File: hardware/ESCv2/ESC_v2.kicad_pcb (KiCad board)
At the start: 4 copper layers, 99.1 x 49.5 mm, 57 parts, among them J1 Conn_02x13_Odd_Even, J2 Conn_01x02, Q1 AON7544, Q2 AON7544, Q3 AON7544, Q4 AON7544, Q5 AON7544, Q6 AON7544, U1 MT6701CT, U2 DRV8305NPHPR

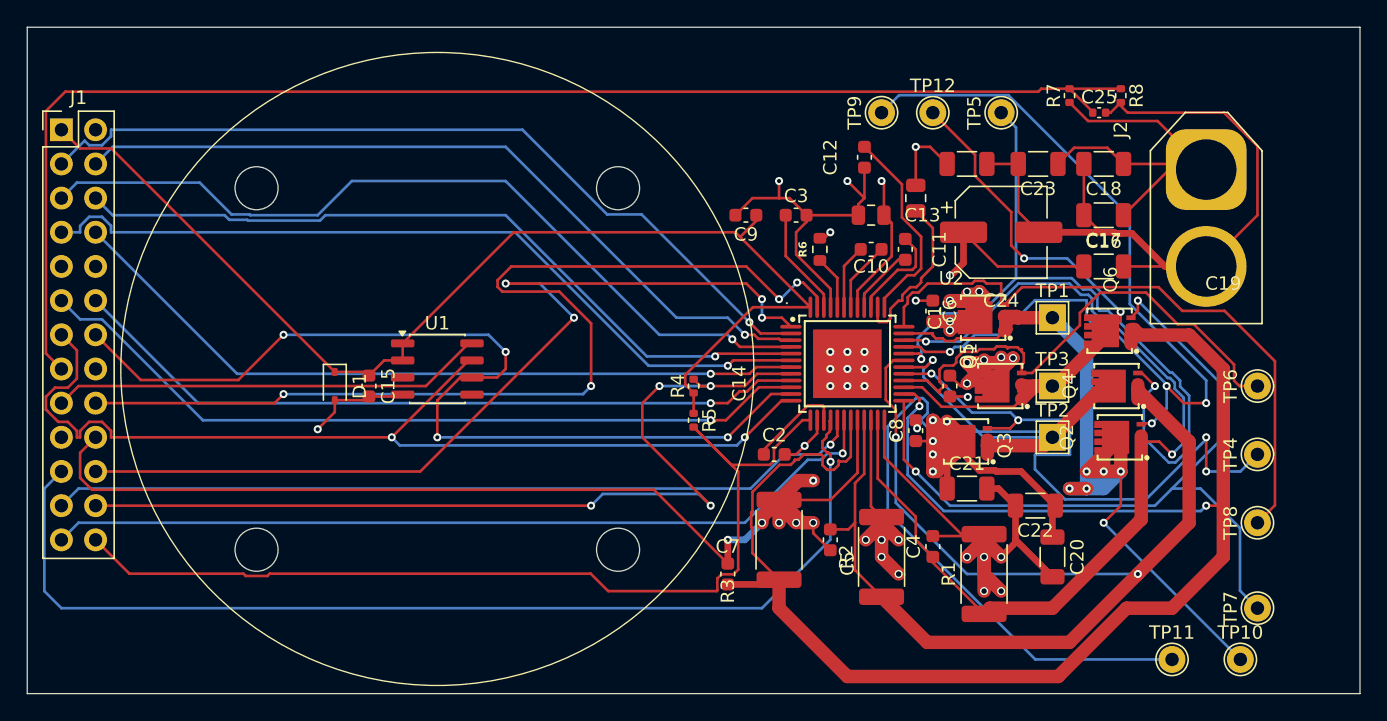
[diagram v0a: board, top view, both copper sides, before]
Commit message: relocating shunts closer to FETs
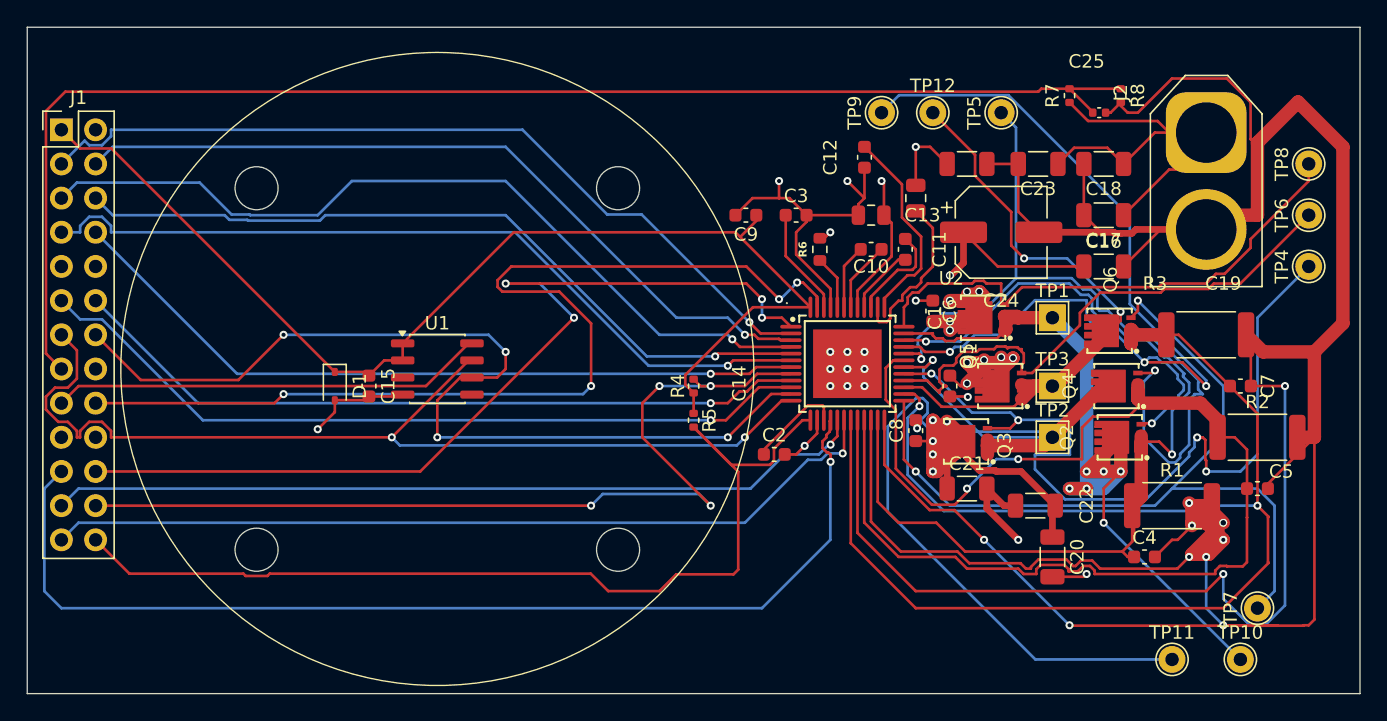
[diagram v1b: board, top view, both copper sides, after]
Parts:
- moved C7 40.6 mm to (138.4, 69.8), turned to 0 degrees
- moved R3 35.2 mm to (135.9, 66.0), turned to 0 degrees
- moved C5 32.0 mm to (139.7, 77.5), turned to 0 degrees
- moved R2 29.3 mm to (139.7, 73.7), turned to 0 degrees
- moved TP8 26.9 mm to (143.5, 53.3)
- moved C4 15.8 mm to (131.3, 82.5), turned to 0 degrees
- moved R1 14.9 mm to (133.3, 78.7), turned to 0 degrees
- moved TP4 14.5 mm to (143.5, 61.0)
- moved TP6 13.3 mm to (143.5, 57.1)
- moved J2 2.75 mm to (135.9, 51.0)
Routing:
- net GND: track 258.9 -> 368.8 mm, vias 32 -> 29
- net /SL_C: track 120.5 -> 103.4 mm
- net /GH_B: track 45.3 -> 61.2 mm
- net /GH_A: track 47.0 -> 39.6 mm
- net /GL_C: track 58.7 -> 62.2 mm
- net /SL_B: track 90.1 -> 93.5 mm
- net /GL_B: track 56.8 -> 59.8 mm
- net /GL_A: track 71.2 -> 74.0 mm
- net /GH_C: track 38.6 -> 41.2 mm
- net /SL_A: track 72.7 -> 74.6 mm
- net +12V: track 130.5 -> 131.3 mm
- net /GPIO_3_PWRGD: track 74.4 -> 73.9 mm

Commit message: improved Kelvin shunts
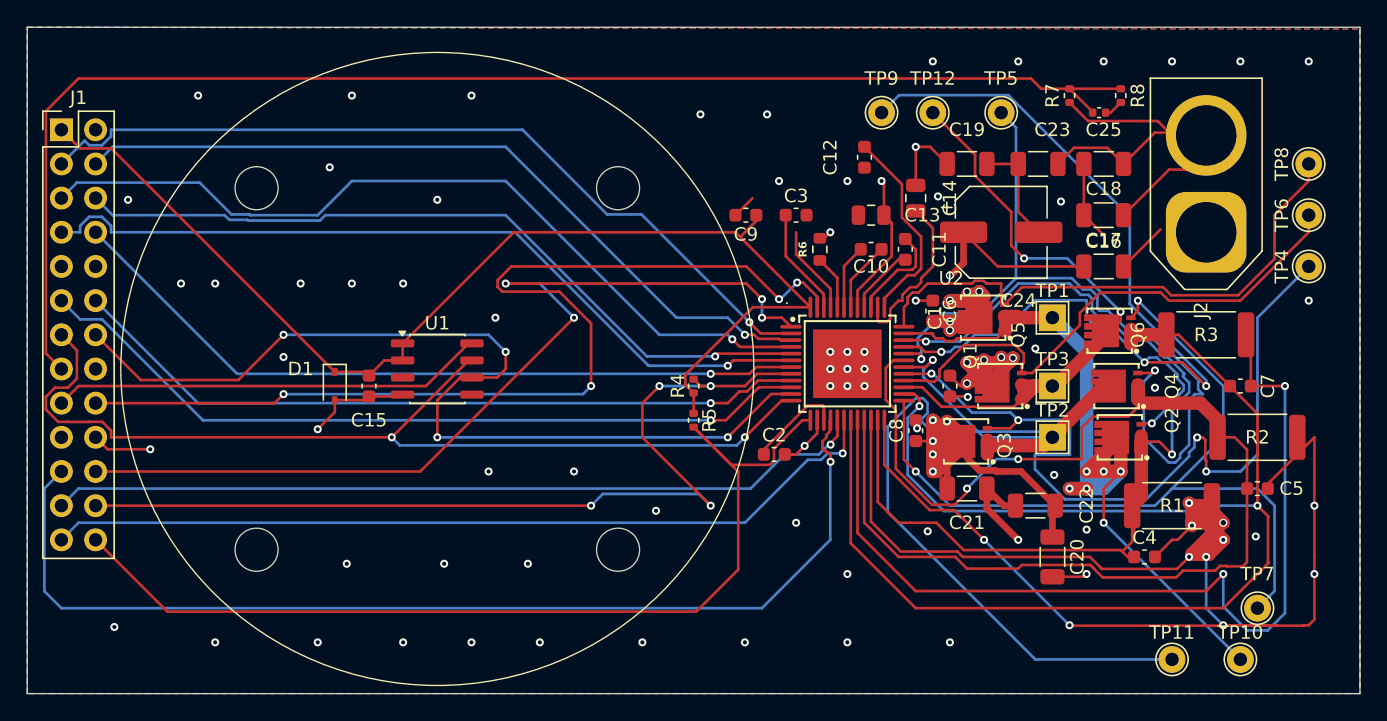
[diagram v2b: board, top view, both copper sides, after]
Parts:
- moved J2 7.41 mm to (135.9, 58.4), turned to 90 degrees
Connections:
- J2 pad 1: +12V -> GND
- J2 pad 2: GND -> +12V
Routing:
- net GND: track 368.8 -> 270.6 mm, vias 29 -> 80
- net /GH_A: track 39.6 -> 41.6 mm
- net /SCLK: track 75.5 -> 74.0 mm
- net /GPIO_3_PWRGD: track 73.9 -> 75.0 mm
- net /GH_C: track 41.2 -> 40.1 mm
- net /Voltage Divider: track 102.7 -> 103.3 mm
- net /SL_B: track 93.5 -> 92.9 mm
- added copper zone on B.Cu, net GND
- added copper zone on F.Cu, net GND

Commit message: Improved kelvin shunts (for real this time), bootstrap caps closer to the DRV chip, added GND pour and a beautiful otter for good luck
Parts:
- added G***: LOGO, GM4108H_Motor_Mount:Otter_footprint1, F.Cu at (104.1, 52.6)
- added G***: LOGO, GM4108H_Motor_Mount:ENPH, F.Cu at (105.3, 88.1)
- added NT1: NetTie_2, NetTie:NetTie-2_SMD_Pad0.5mm, F.Cu at (139.6, 66.0)
- added NT2: NetTie_2, NetTie:NetTie-2_SMD_Pad0.5mm, F.Cu at (137.2, 78.7)
- added NT3: NetTie_2, NetTie:NetTie-2_SMD_Pad0.5mm, F.Cu at (142.6, 75.4)
- moved C12 7.77 mm to (113.9, 59.8)
- moved C11 2.24 mm to (112.0, 61.3), turned to -90 degrees
- moved C10 2.06 mm to (109.6, 61.2), turned to -90 degrees
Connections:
- U2 pad 20: GND -> /SP3
- U2 pad 22: GND -> /SP2
- U2 pad 24: GND -> /SP1
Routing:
- net GND: track 270.6 -> 130.9 mm, vias 80 -> 87
- net /SP3: track 0.00 -> 66.6 mm, vias 0 -> 2
- net /SP2: track 0.00 -> 51.3 mm, vias 0 -> 2
- net /SP1: track 0.00 -> 37.0 mm, vias 0 -> 2
- net Net-(U2-VCP_LSD): track 15.1 -> 5.76 mm
- net Net-(U2-CP2H): track 7.41 -> 2.31 mm
- net /SL_A: track 74.6 -> 71.3 mm
- net Net-(U2-CP1L): track 5.25 -> 2.06 mm
- net /SH_A: track 67.9 -> 69.6 mm
- net /GL_B: track 59.8 -> 58.5 mm
- net Net-(U2-CP2L): track 5.10 -> 4.06 mm
- net Net-(U2-CP1H): track 4.81 -> 3.98 mm
- net /ADC3: track 63.2 -> 63.8 mm
- net /SL_C: track 103.4 -> 103.9 mm
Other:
- board text added: "+"
- board text added: "-"
- board text added: "A"
- board text added: "B"
- board text added: "C"
- board text added: "Theodore Price-Parsons Custom FOC ESC - v1"
